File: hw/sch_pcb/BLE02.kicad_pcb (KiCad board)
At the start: 2 copper layers, 40.1 x 30 mm, 26 parts, among them J1 Conn_Coaxial, J2 3.3-5V, M1 HOLE, M2 HOLE, M3 HOLE, M4 HOLE, U5 CC2564CRVMR, Y3 ECS-260-8-36CKM-TR

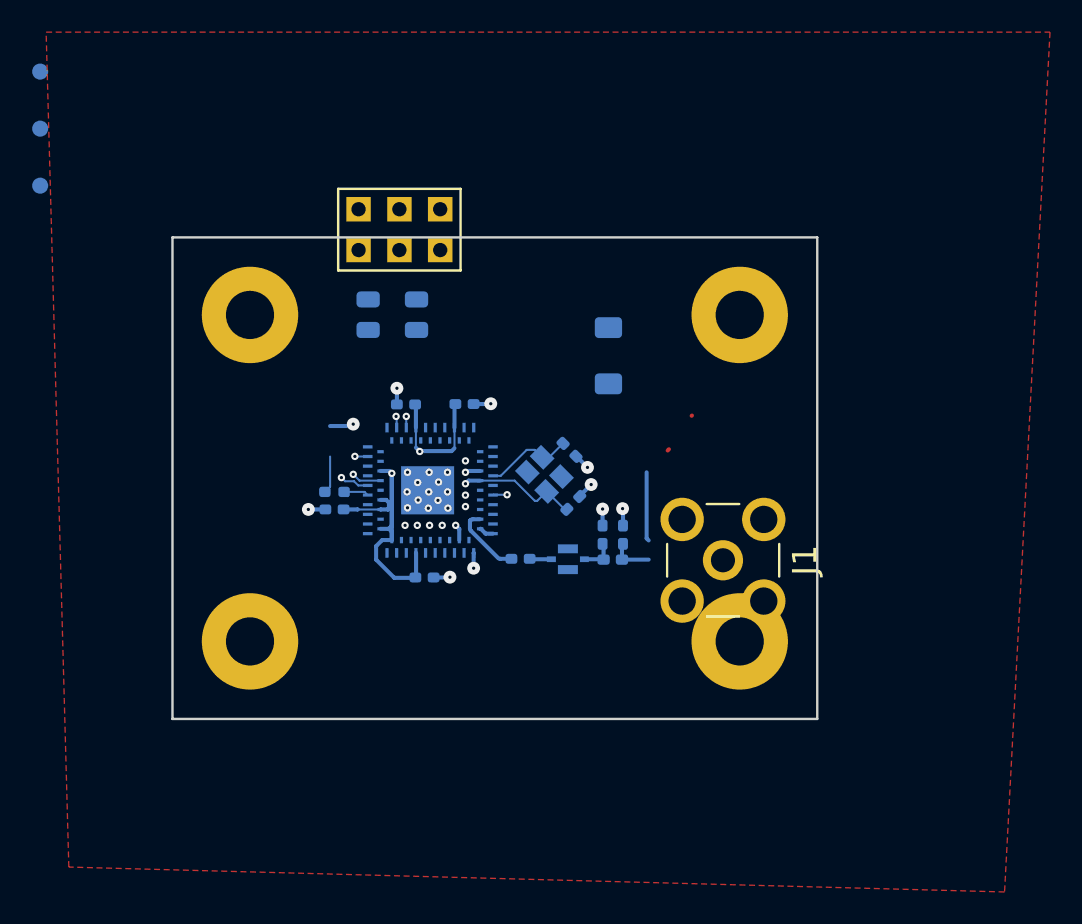
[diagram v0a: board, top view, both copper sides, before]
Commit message: Connectors placement on the board
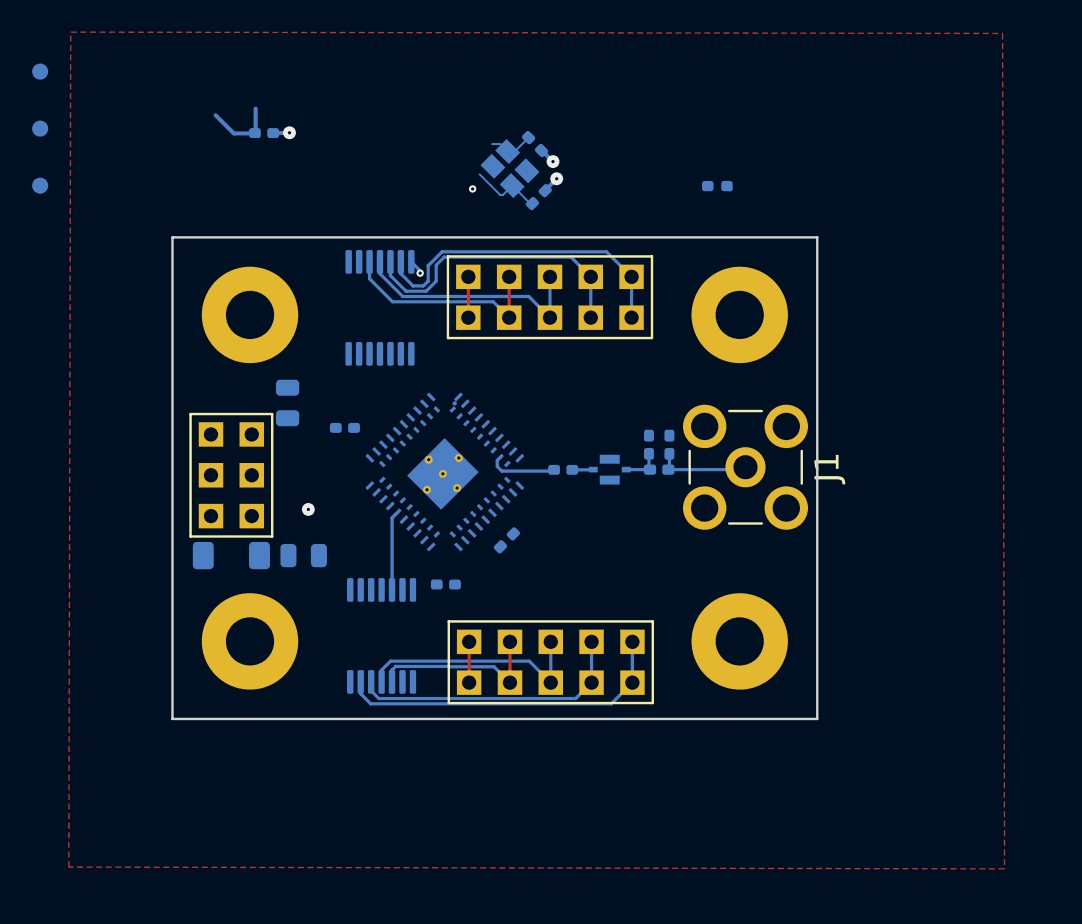
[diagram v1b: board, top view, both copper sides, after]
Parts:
- removed U5: CC2564CRVMR, cc2654-board-footprints:CC2564CRVMR
- added J3: JUMP_5X2, Mlab_Pin_Headers:Straight_2x05, F.Cu at (152.0, 116.5)
- added J4: JUMP_5X2, Mlab_Pin_Headers:Straight_2x05, F.Cu at (151.9, 93.7)
- added U1: TXS0104EPW, Package_SO:TSSOP-14_4.4x5mm_P0.65mm, B.Cu at (141.3, 94.4)
- added U2: CC2564CRVMR, MLAB_Lib:RVM0076A, B.Cu at (145.4, 104.6)
- added U3: TXS0104EPW, Package_SO:TSSOP-14_4.4x5mm_P0.65mm, B.Cu at (141.4, 114.8)
- moved R18 30.5 mm to (162.3, 86.8)
- moved C23 29.4 mm to (134.1, 83.5)
- moved D3 26.6 mm to (132.1, 109.8), turned to 180 degrees
- moved C25 19.2 mm to (151.2, 87.5)
- moved Y3 19.2 mm to (149.4, 85.7)
- moved C26 19.2 mm to (151.0, 84.2)
- moved J2 18.5 mm to (132.1, 104.8), turned to 0 degrees
- moved C16 16.6 mm to (136.6, 109.8), turned to 0 degrees
- moved C24 8.89 mm to (149.2, 108.9), turned to 45 degrees
- moved C21 8.36 mm to (145.4, 111.6)
- moved C17 7.44 mm to (135.6, 100.3)
- moved C18 6.30 mm to (158.1, 102.9)
- moved C19 6.30 mm to (159.4, 102.9)
- moved L2 6.30 mm to (158.7, 104.5)
- moved FL1 6.15 mm to (155.7, 104.5)
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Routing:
- net VDD_1V8: track 28.9 -> 4.50 mm, vias 2 -> 0
- net Net-(U3-B1): track 0.00 -> 21.0 mm
- net Net-(U1-B1): track 0.00 -> 20.0 mm
- net Net-(U1-B2): track 0.00 -> 18.2 mm
- net Net-(U3-B2): track 0.00 -> 17.4 mm
- net Net-(U1-B3): track 0.00 -> 15.0 mm
- net Net-(U3-B3): track 0.00 -> 14.6 mm
- net GND: track 21.3 -> 7.62 mm, vias 33 -> 4
- net Net-(U1-B4): track 0.00 -> 13.3 mm
- net Net-(U3-B4): track 0.00 -> 11.1 mm
- net (no net): track 4.40 -> 0.00 mm
- net Net-(J1-In): track 2.67 -> 5.91 mm
- net USART2_TX_1V8: track 1.84 -> 4.93 mm, vias 1 -> 0
- net Net-(U2A-XTALM_FREFM): track 5.58 -> 2.82 mm
- net Net-(J4-2-Pad1): track 0.00 -> 2.54 mm
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
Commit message: Fix footprint of pin-headers.
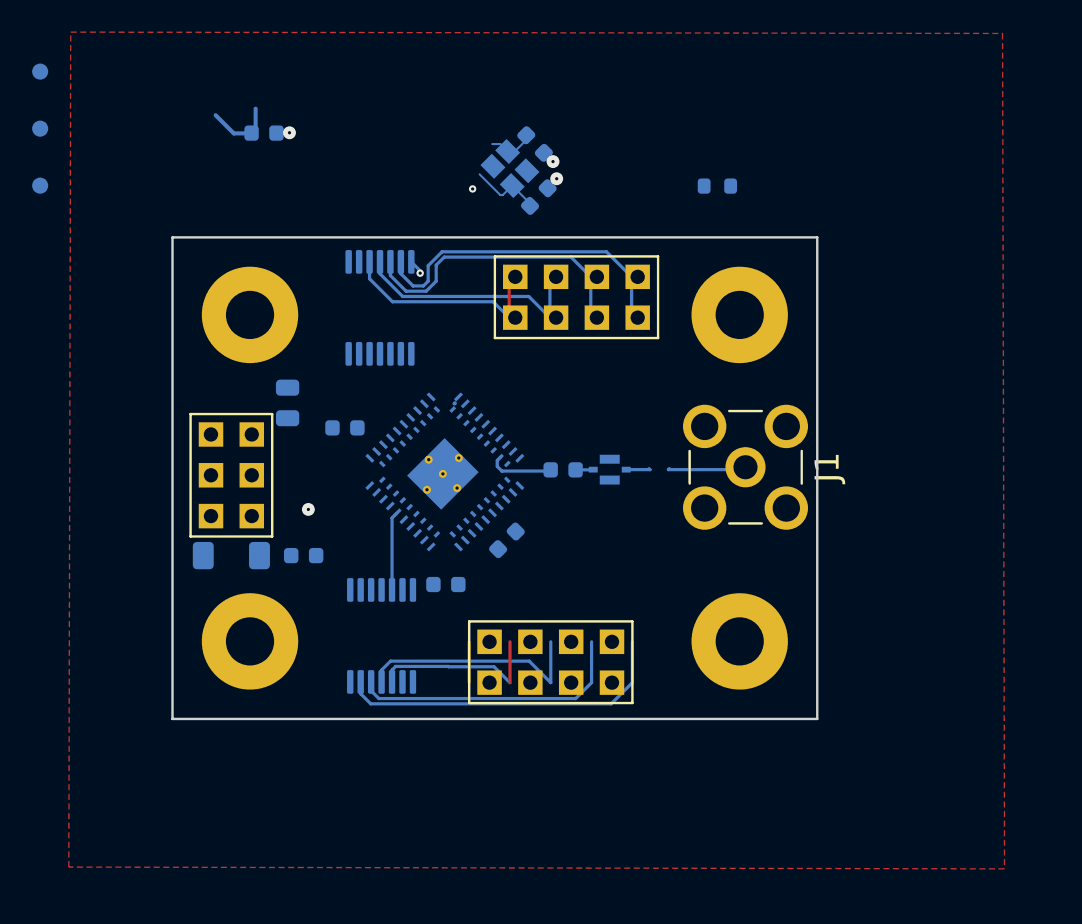
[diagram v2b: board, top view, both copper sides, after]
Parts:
- removed C18, C19: DNP, Capacitor_SMD:C_0402_1005Metric_Pad0.74x0.62mm_HandSolder
- removed L2: 0ohm, Inductor_SMD:L_0402_1005Metric_Pad0.77x0.64mm_HandSolder
- C16: footprint Capacitor_SMD:C_0805_2012Metric -> Capacitor_SMD:C_0603_1608Metric
- C20, C21, C22, C23, C24, C25, C26: footprint Capacitor_SMD:C_0402_1005Metric_Pad0.74x0.62mm_HandSolder -> Capacitor_SMD:C_0603_1608Metric
- J3, J4: footprint Mlab_Pin_Headers:Straight_2x05 -> Mlab_Pin_Headers:Straight_2x04
- R18: footprint Resistor_SMD:R_0402_1005Metric_Pad0.72x0.64mm_HandSolder -> Resistor_SMD:R_0603_1608Metric
- moved J4 1.65 mm to (153.6, 93.7)
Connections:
- C25 pad 2: GND -> Net-(U2A-XTALP_FREFP)
- J1 pad 1: Net-(J1-In) -> Net-(FL1-OUT)
- J3 pad 1: Net-(J3-2-Pad1) -> Net-(U3-B4)
- J3 pad 2: Net-(J3-2-Pad1) -> Net-(U3-B4)
- J3 pad 3: Net-(U3-B4) -> Net-(U3-B3)
- J3 pad 4: Net-(U3-B4) -> Net-(U3-B3)
- J3 pad 5: Net-(U3-B3) -> Net-(U3-B2)
- J3 pad 6: Net-(U3-B3) -> Net-(U3-B2)
- J3 pad 7: Net-(U3-B2) -> Net-(U3-B1)
- J3 pad 8: Net-(U3-B2) -> Net-(U3-B1)
- J4 pad 1: Net-(J4-2-Pad1) -> Net-(U1-B4)
- J4 pad 2: Net-(J4-2-Pad1) -> Net-(U1-B4)
- J4 pad 3: Net-(U1-B4) -> Net-(U1-B3)
- J4 pad 4: Net-(U1-B4) -> Net-(U1-B3)
- J4 pad 5: Net-(U1-B3) -> Net-(U1-B2)
- J4 pad 6: Net-(U1-B3) -> Net-(U1-B2)
- J4 pad 7: Net-(U1-B2) -> Net-(U1-B1)
- J4 pad 8: Net-(U1-B2) -> Net-(U1-B1)
- U1 pad 2: unconnected-(U1-A1-Pad2) -> AUD_OUT
- U1 pad 3: unconnected-(U1-A2-Pad3) -> AUD_IN
- U1 pad 4: unconnected-(U1-A3-Pad4) -> AUD_CLK
- U1 pad 5: unconnected-(U1-A4-Pad5) -> AUD_FSYNC
- U2 pad A35: unconnected-(U2A-AUD_FSYNC-PadA35) -> AUD_FSYNC
- U2 pad B32: unconnected-(U2A-AUD_CLK-PadB32) -> AUD_CLK
- U2 pad B33: unconnected-(U2A-AUD_OUT-PadB33) -> AUD_OUT
- U2 pad B34: unconnected-(U2A-AUD_IN-PadB34) -> AUD_IN
- U2 pad B4: GND -> Net-(U2A-XTALP_FREFP)
- U3 pad 2: USART2_RTS_1V8 -> USART2_RX_1V8
- U3 pad 4: USART2_RX_1V8 -> USART2_RTS_1V8
- Y3 pad 1: GND -> Net-(U2A-XTALP_FREFP)
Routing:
- net Net-(J1-In): track 5.91 -> 0.00 mm
- net Net-(U2A-XTALP_FREFP): track 0.00 -> 4.53 mm
- net GND: track 7.62 -> 3.09 mm
- net Net-(FL1-OUT): track 2.48 -> 6.56 mm
- net Net-(U3-B4): track 11.1 -> 13.7 mm
- net Net-(J4-2-Pad1): track 2.54 -> 0.00 mm
- net Net-(J3-2-Pad1): track 2.54 -> 0.00 mm

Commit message: Add text for connectors
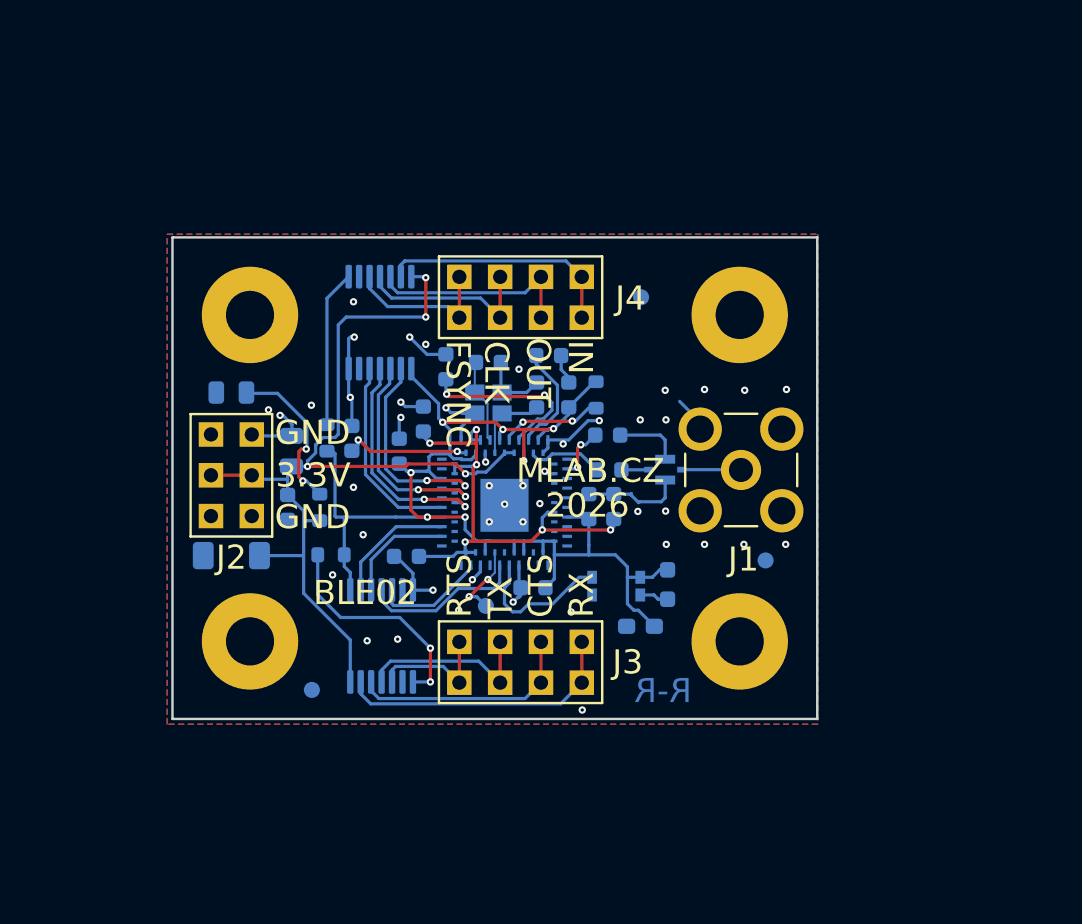
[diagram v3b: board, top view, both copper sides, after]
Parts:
- removed R18: 0, Resistor_SMD:R_0603_1608Metric
- added C1: 0.1uF, Capacitor_SMD:C_0603_1608Metric, B.Cu at (143.0, 109.9)
- added C2: 0.1uF, Capacitor_SMD:C_0603_1608Metric, B.Cu at (144.1, 101.3)
- added C3: 0.1uF, Capacitor_SMD:C_0603_1608Metric, B.Cu at (155.9, 106.8)
- added C4: 0.1uF, Capacitor_SMD:C_0603_1608Metric, B.Cu at (155.5, 102.3)
- added C5: 0.1uF, Capacitor_SMD:C_0603_1608Metric, B.Cu at (145.4, 98.1)
- added C6: 0.1uF, Capacitor_SMD:C_0603_1608Metric, B.Cu at (151.8, 97.4)
- added C7: 0.1uF, Capacitor_SMD:C_0603_1608Metric, B.Cu at (139.6, 102.5)
- added C8: 100nF/50V, Capacitor_SMD:C_0603_1608Metric_Pad1.08x0.95mm_HandSolder, B.Cu at (157.6, 114.2)
- added D1: LED, LED_SMD:LED_0805_2012Metric, B.Cu at (132.1, 99.7)
- added R1: 10k, Resistor_SMD:R_0603_1608Metric, B.Cu at (154.8, 99.8)
- added R2: 10k, Resistor_SMD:R_0603_1608Metric, B.Cu at (138.1, 102.5)
- added R3: 10k, Resistor_SMD:R_0603_1608Metric, B.Cu at (138.3, 109.8)
- added R4: 2k2, Resistor_SMD:R_0603_1608Metric, B.Cu at (137.6, 106.8)
- added R5: 10k, Resistor_SMD:R_0603_1608Metric_Pad0.98x0.95mm_HandSolder, B.Cu at (159.2, 111.6)
- added TP1: TestPoint, TestPoint:TestPoint_Pad_D1.0mm, B.Cu at (147.9, 113.0)
- added X1: ASH7K-32.768KHZ-T, MLAB_Lib:ASH7K_ABR, B.Cu at (156.1, 111.7)
- moved FID3 54.4 mm to (165.3, 110.1)
- moved FID2 38.8 mm to (157.6, 93.7)
- moved FID1 35.7 mm to (137.1, 118.2)
- moved C23 32.9 mm to (150.9, 111.8), turned to 180 degrees
- moved Y3 14.7 mm to (148.1, 100.3), turned to 180 degrees
- moved C21 14.1 mm to (153.1, 99.8), turned to 90 degrees
- moved C26 13.9 mm to (148.1, 97.8), turned to 180 degrees
- moved C25 12.3 mm to (151.1, 99.8), turned to -90 degrees
- moved C24 5.52 mm to (154.3, 106.8), turned to 90 degrees
- moved U2 4.17 mm to (149.1, 106.5), turned to -90 degrees
- moved C22 3.68 mm to (142.6, 103.3), turned to 90 degrees
- moved J4 3.48 mm to (150.1, 93.7)
- moved FL1 3.45 mm to (159.1, 104.5)
- moved C16 3.16 mm to (135.6, 106.8), turned to -90 degrees
- moved C17 3.01 mm to (135.8, 103.3)
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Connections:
- U1 pad 1: unconnected-(U1-V_{CCA}-Pad1) -> VDD_1V8
- U1 pad 14: unconnected-(U1-V_{CCB}-Pad14) -> VCC
- U1 pad 2: AUD_OUT -> AUD_IN
- U1 pad 3: AUD_IN -> AUD_OUT
- U1 pad 8: unconnected-(U1-OE-Pad8) -> Net-(U1-OE)
- U2 pad A12: unconnected-(U2A-DCO_LDO_OUT-PadA12) -> Net-(U2A-DCO_LDO_OUT)
- U2 pad A2: unconnected-(U2A-DIG_LDO_OUT-PadA2) -> Net-(C1-Pad1)
- U2 pad A3: unconnected-(U2A-DIG_LDO_OUT-PadA3) -> Net-(C1-Pad1)
- U2 pad A6: NSHUTDOWN_1V8 -> Net-(U2A-SHUTD_N)
- U2 pad A7: unconnected-(U2A-CL1.5_LDO_OUT-PadA7) -> Net-(U2A-CL1.5_LDO_OUT)
- U2 pad A8: unconnected-(U2A-ADC_PPA_LDO_OUT-PadA8) -> Net-(U2A-ADC_PPA_LDO_OUT)
- U2 pad B1: unconnected-(U2A-SRAM_LDO_OUT-PadB1) -> Net-(U2A-SRAM_LDO_OUT)
- U2 pad B15: unconnected-(U2A-DIG_LDO_OUT-PadB15) -> Net-(C1-Pad1)
- U2 pad B24: BT_TX_DBG -> Net-(U2A-TX_DBG)
- U2 pad B26: unconnected-(U2A-DIG_LDO_OUT-PadB26) -> Net-(C1-Pad1)
- U2 pad B27: unconnected-(U2A-DIG_LDO_OUT-PadB27) -> Net-(C1-Pad1)
- U2 pad B35: unconnected-(U2A-DIG_LDO_OUT-PadB35) -> Net-(C1-Pad1)
- U2 pad B36: unconnected-(U2A-DIG_LDO_OUT-PadB36) -> Net-(C1-Pad1)
- U3 pad 1: unconnected-(U3-V_{CCA}-Pad1) -> VDD_1V8
- U3 pad 14: unconnected-(U3-V_{CCB}-Pad14) -> VCC
- U3 pad 4: USART2_RTS_1V8 -> USART2_TX_1V8
- U3 pad 5: USART2_TX_1V8 -> USART2_RTS_1V8
- U3 pad 8: unconnected-(U3-OE-Pad8) -> Net-(U3-OE)
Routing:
- net VDD_1V8: track 4.50 -> 80.5 mm, vias 0 -> 7
- net VCC: track 0.00 -> 57.6 mm, vias 0 -> 4
- net GND: track 3.09 -> 51.8 mm, vias 4 -> 45
- net Net-(C1-Pad1): track 0.00 -> 30.3 mm, vias 0 -> 6
- net AUD_CLK: track 0.00 -> 14.1 mm, vias 0 -> 2
- net Net-(U3-OE): track 0.00 -> 14.0 mm, vias 0 -> 2
- net AUD_OUT: track 0.00 -> 13.7 mm, vias 0 -> 2
- net AUD_IN: track 0.00 -> 13.0 mm, vias 0 -> 2
- net AUD_FSYNC: track 0.00 -> 12.3 mm
- net Net-(U2A-CL1.5_LDO_OUT): track 0.00 -> 11.2 mm, vias 0 -> 2
- net Net-(D1-A): track 0.00 -> 10.1 mm, vias 0 -> 2
- net Net-(U1-OE): track 0.00 -> 9.77 mm
- net BT_SLOW_CLK: track 0.29 -> 9.07 mm
- net Net-(U2A-SRAM_LDO_OUT): track 0.00 -> 7.91 mm, vias 0 -> 2
- net USART2_RX_1V8: track 0.00 -> 7.70 mm
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- added copper zone on B.Cu, net GND
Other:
- board text added: "2026"
- board text added: "3.3V"
- board text added: "BLE02"
- board text added: "CLK"
- board text added: "CTS"
- board text added: "FSYNC"
- board text added: "GND"
- board text added: "IN"
- board text added: "MLAB.CZ"
- board text added: "OUT"
- board text added: "R-R"
- board text added: "RTS"
- board text added: "RX"
- board text added: "TX"

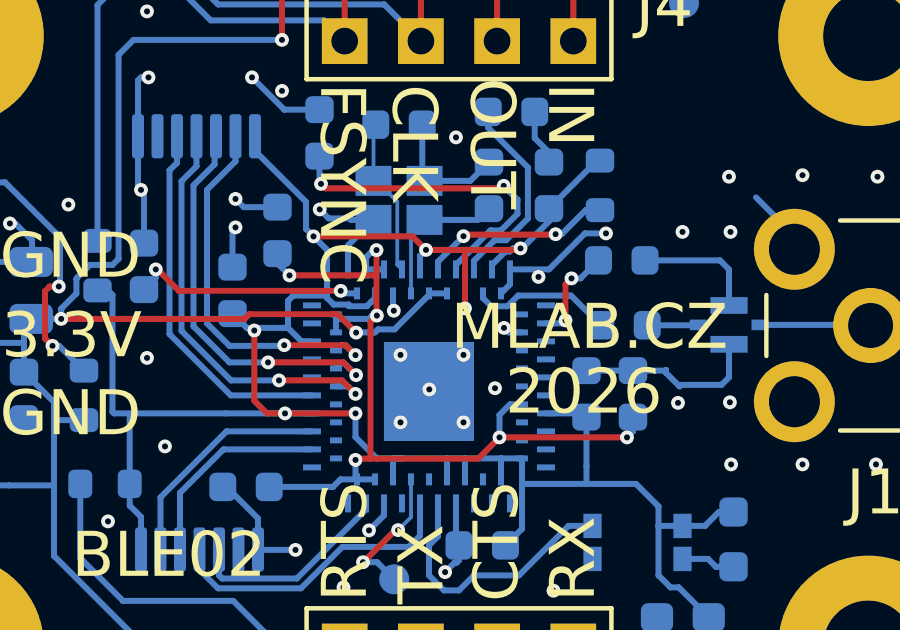
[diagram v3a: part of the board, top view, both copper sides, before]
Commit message: Connect B10 to gnd
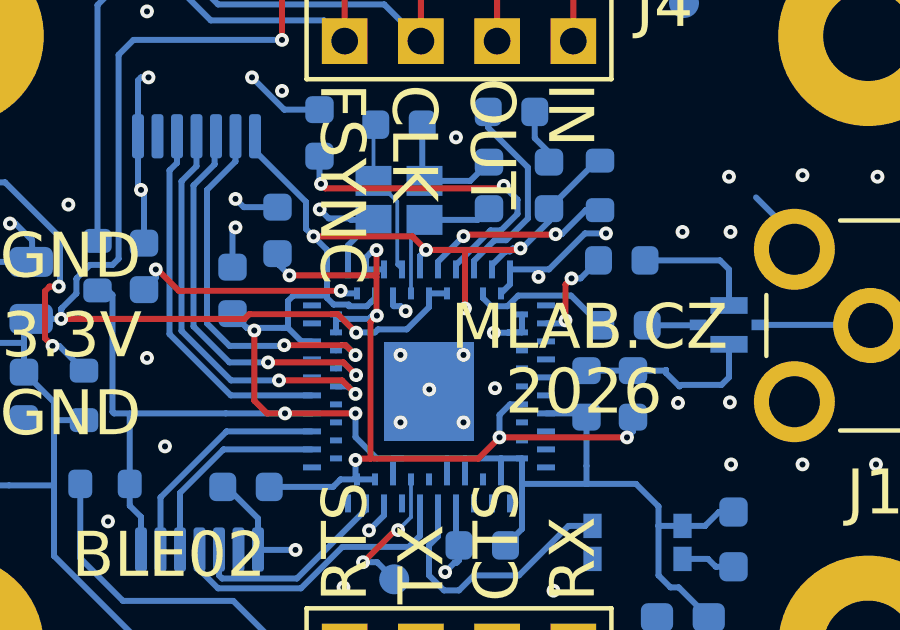
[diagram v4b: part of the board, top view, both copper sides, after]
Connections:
- U2 pad B10: unconnected-(U2B-NC-PadB10) -> GND
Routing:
- net GND: track 51.8 -> 53.2 mm

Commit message: Improve layout.
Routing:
- net VDD_1V8: track 80.5 -> 78.9 mm
- net Net-(C1-Pad1): track 30.3 -> 29.2 mm
- net GND: track 53.2 -> 52.4 mm
- net Net-(U1-B3): track 11.4 -> 10.8 mm
- net Net-(U1-B2): track 13.1 -> 12.5 mm
- net Net-(U3-B2): track 14.3 -> 13.7 mm
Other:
- board text added: "BLE02A"
- board text removed: "BLE02"
